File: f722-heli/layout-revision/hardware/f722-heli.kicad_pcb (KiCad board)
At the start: 6 copper layers, 41.7 x 25.4 mm, 156 parts, among them J1 USB4145-03-0170-C, J10 PORT B / JST GH, J11 PORT C / JST GH, J12 DSM / JST ZH, J2 S1 / GND-VX-S, J3 S2 / GND-VX-S, J4 S3 / GND-VX-S, J5 TAIL / GND-VX-S, J6 ESC / GND-VX-S, J7 RPM / GND-VX-S, J8 SBUS / GND-VX-S, J9 PORT A / JST GH, Q1 BSS138LT1G, Q2 BSS138LT1G, SW1 BOOT / KMT031NGJLHS, U1 STM32F722RET6, U10 TPS2553DRVR / USB input limit, U11 TPS2553DRVR / DSM output limit, U12 USBLC6-4SC6 / header clamp, U13 USBLC6-4SC6 / header clamp, U14 TPD4E05U06DQAR / UART ESD, U15 TPD4E05U06DQAR / UART ESD, U16 PESD15VS2UT,215 / 15V ESD, U2 ICM-42688-P, U3 W25N01GVZEIG / 128MiB, U4 DPS368XTSA1 / 0x76, U5 TPS259472ARPWR, U6 TPS63070RNMR / nominal 5.088V, U7 TPS2117DRLR / ABC priority mux, U8 TPS2121RUXR / BEC-priority co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, U9 TPS62162DSGR / 3.3V 1A, Y1 8MHz / CL10pF / TAXM8M4RDBCCT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

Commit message: WIP: checkpoint F722 routing at 49 unfinished connections
Six actual protected channels complete. Current numerical power/VCAP validation pending. Not ready for fabrication or flight.
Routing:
- net SERVO2_MCU: track 0.00 -> 35.8 mm, vias 0 -> 4
- net PORT_C_TX_EXT: track 0.00 -> 19.9 mm, vias 0 -> 2
- net FLASH_HOLD_N: track 0.00 -> 13.4 mm, vias 0 -> 2
- net TAIL_EXT: track 0.00 -> 9.80 mm, vias 0 -> 1
- net PORT_A_TX_EXT: track 0.84 -> 9.07 mm

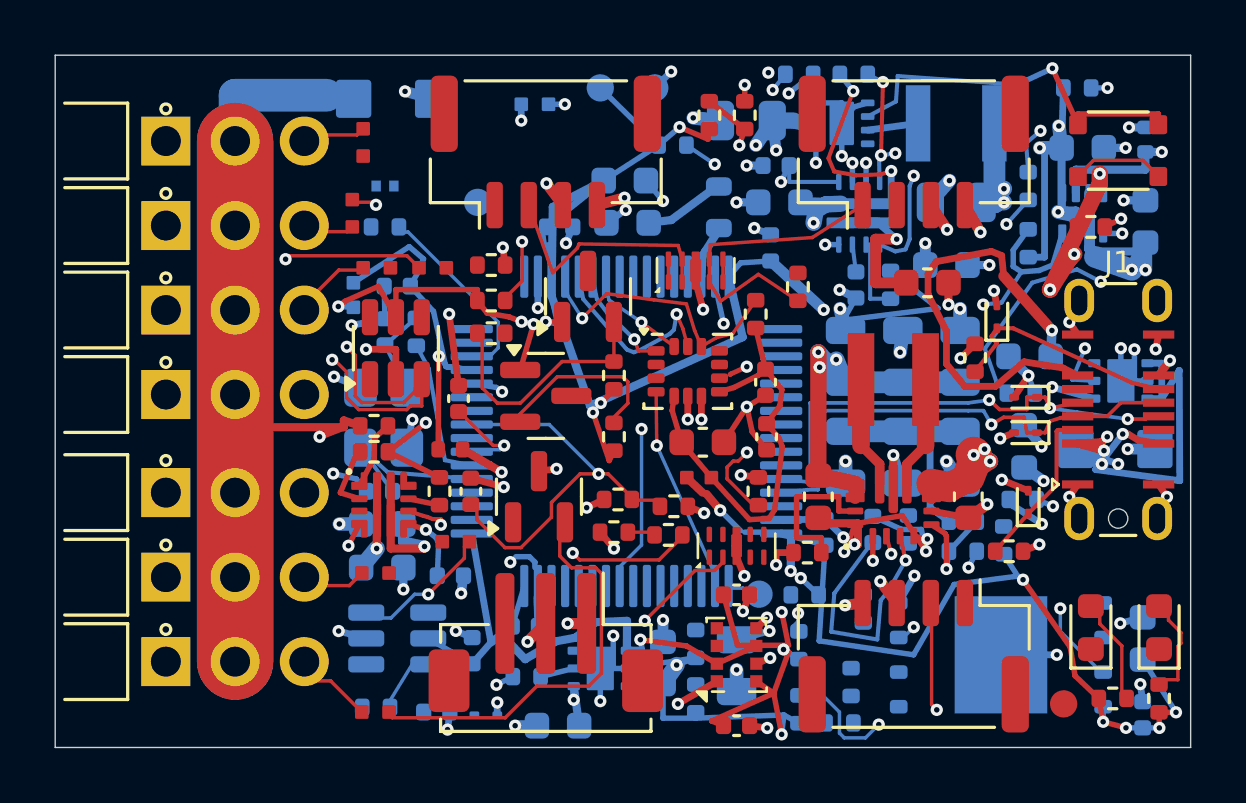
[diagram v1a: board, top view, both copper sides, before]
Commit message: WIP: checkpoint F722 routing at 45 unfinished connections
Native geometry and strict parity clean. Current numerical power/VCAP validation pending. Not ready for fabrication or flight.
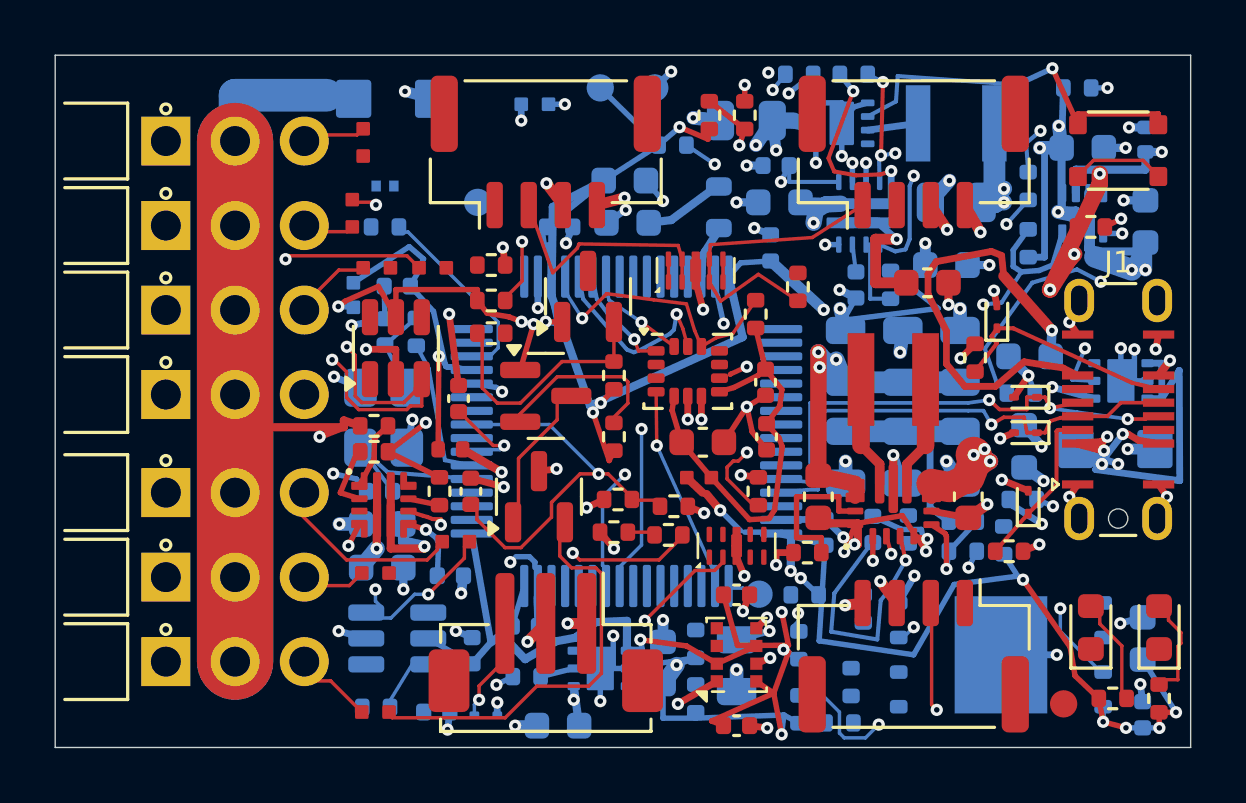
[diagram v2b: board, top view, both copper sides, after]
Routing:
- net ESC_MCU: track 4.39 -> 20.0 mm, vias 1 -> 3
- net ESC_EXT: track 0.00 -> 6.14 mm
- net RPM_HV: track 0.00 -> 4.35 mm
- net DSM_RX_EXT: track 0.00 -> 2.18 mm, vias 0 -> 1
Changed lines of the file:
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@@
+	)
+	(segment
+		(start 16.99961 14.7916)
+		(end 16.99961 16.50142)
+		(width 0.127)
+		(layer "F.Cu")
+		(net "RPM_HV")
+	)
+	(segment
+		(start 16.99961 14.7916)
+		(end 18.41752 13.37369)
+		(width 0.127)
+		(layer "F.Cu")
+		(net "RPM_HV")
+	)
+	(segment
+		(start 18.41752 12.73646)
+		(end 18.41752 13.37369)
+		(width 0.127)
+		(layer "F.Cu")
+		(net "RPM_HV")
 	)
 	(segment
@@
 	)
 	(segment
+		(start 10.68786 18.51864)
+		(end 13.64937 18.51864)
+		(width 0.127)
+		(layer "F.Cu")
+		(net "ESC_EXT")
+	)
+	(segment
+		(start 8.88966 16.72044)
+		(end 10.68786 18.51864)
+		(width 0.127)
+		(layer "F.Cu")
+		(net "ESC_EXT")
+	)
+	(segment
+		(start 13.64937 18.51864)
+		(end 14.01354 18.15447)
+		(width 0.127)
+		(layer "F.Cu")
+		(net "ESC_EXT")
+	)
+	(segment
+		(start 14.01354 18.03646)
+		(end 14.01354 18.15447)
+		(width 0.127)
+		(layer "F.Cu")
+		(net "ESC_EXT")
+	)
+	(segment
 		(start 15.01354 18.03646)
 		(end 15.01354 18.45397)
@@
 	)
 	(via
+		(at 11.75059 19.60158)
+		(size 0.45)
+		(drill 0.2)
+		(layers "F.Cu" "B.Cu")
+		(tenting
+			(front yes)
+			(back yes)
+		)
+		(net "ESC_MCU")
+	)
+	(via
+		(at 20.90574 15.38266)
+		(size 0.45)
+		(drill 0.2)
+		(layers "F.Cu" "B.Cu")
+		(tenting
+			(front yes)
+			(back yes)
+		)
+		(net "ESC_MCU")
+	)
+	(via
 		(at 13.68751 19.78)
 		(size 0.45)
@@
 		(width 0.127)
 		(layer "B.Cu")
+		(net "ESC_MCU")
+	)
+	(segment
+		(start 20.08099 18.71362)
+		(end 20.13148 18.76411)
+		(width 0.127)
+		(layer "B.Cu")
+		(net "ESC_MCU")
+	)
+	(segment
+		(start 20.08099 16.20741)
+		(end 20.08099 18.71362)
+		(width 0.127)
+		(layer "B.Cu")
+		(net "ESC_MCU")
+	)
+	(segment
+		(start 11.75059 19.60158)
+		(end 11.75059 20.02972)
+		(width 0.127)
+		(layer "B.Cu")
+		(net "ESC_MCU")
+	)
+	(segment
+		(start 11.75059 20.02972)
+		(end 11.97126 20.25039)
+		(width 0.127)
+		(layer "B.Cu")
+		(net "ESC_MCU")
+	)
+	(segment
+		(start 20.08099 16.20741)
+		(end 20.90574 15.38266)
+		(width 0.127)
+		(layer "B.Cu")
+		(net "ESC_MCU")
+	)
+	(segment
+		(start 17.40836 19.18389)
+		(end 18.74475 17.8475)
+		(width 0.127)
+		(layer "In2.Cu")
+		(net "ESC_MCU")
+	)
+	(segment
+		(start 12.16828 19.18389)
+		(end 17.40836 19.18389)
+		(width 0.127)
+		(layer "In2.Cu")
+		(net "ESC_MCU")
+	)
+	(segment
+		(start 18.74475 17.8475)
+		(end 18.84039 17.8475)
+		(width 0.127)
+		(layer "In2.Cu")
+		(net "ESC_MCU")
+	)
+	(segment
+		(start 11.75059 19.60158)
+		(end 12.16828 19.18389)
+		(width 0.127)
+		(layer "In2.Cu")
+		(net "ESC_MCU")
+	)
+	(segment
+		(start 20.90574 15.38266)
+		(end 20.90574 15.78215)
+		(width 0.127)
+		(layer "In2.Cu")
+		(net "ESC_MCU")
+	)
+	(segment
+		(start 18.84039 17.8475)
+		(end 20.90574 15.78215)
+		(width 0.127)
+		(layer "In2.Cu")
 		(net "ESC_MCU")
 	)
@@
 	)
 	(segment
+		(start 16.18311 22.50946)
+		(end 16.34054 22.50946)
+		(width 0.127)
+		(layer "F.Cu")
+		(net "DSM_RX_EXT")
+	)
+	(segment
+		(start 15.55286 23.13971)
+		(end 16.18311 22.50946)
+		(width 0.127)
+		(layer "F.Cu")
+		(net "DSM_RX_EXT")
+	)
+	(segment
+		(start 15.55286 23.13971)
+		(end 15.55286 23.65162)
+		(width 0.127)
+		(layer "F.Cu")
+		(net "DSM_RX_EXT")
+	)
+	(via
+		(at 15.55286 23.65162)
+		(size 0.45)
+		(drill 0.2)
+		(layers "F.Cu" "B.Cu")
+		(tenting
+			(front yes)
+			(back yes)
+		)
+		(net "DSM_RX_EXT")
+	)
+	(segment
+		(start 15.38 23.82448)
+		(end 15.38 24.2)
+		(width 0.127)
+		(layer "B.Cu")
+		(net "DSM_RX_EXT")
+	)
+	(segment
+		(start 15.38 23.82448)
+		(end 15.55286 23.65162)
+		(width 0.127)
+		(layer "B.Cu")
+		(net "DSM_RX_EXT")
+	)
+	(segment

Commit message: WIP: checkpoint F722 routing at 14 unfinished connections
Corrected supply-terminal model documented. Current numerical power/VCAP validation pending; historical USB/DSM results invalid. Not for manufacture or flight.
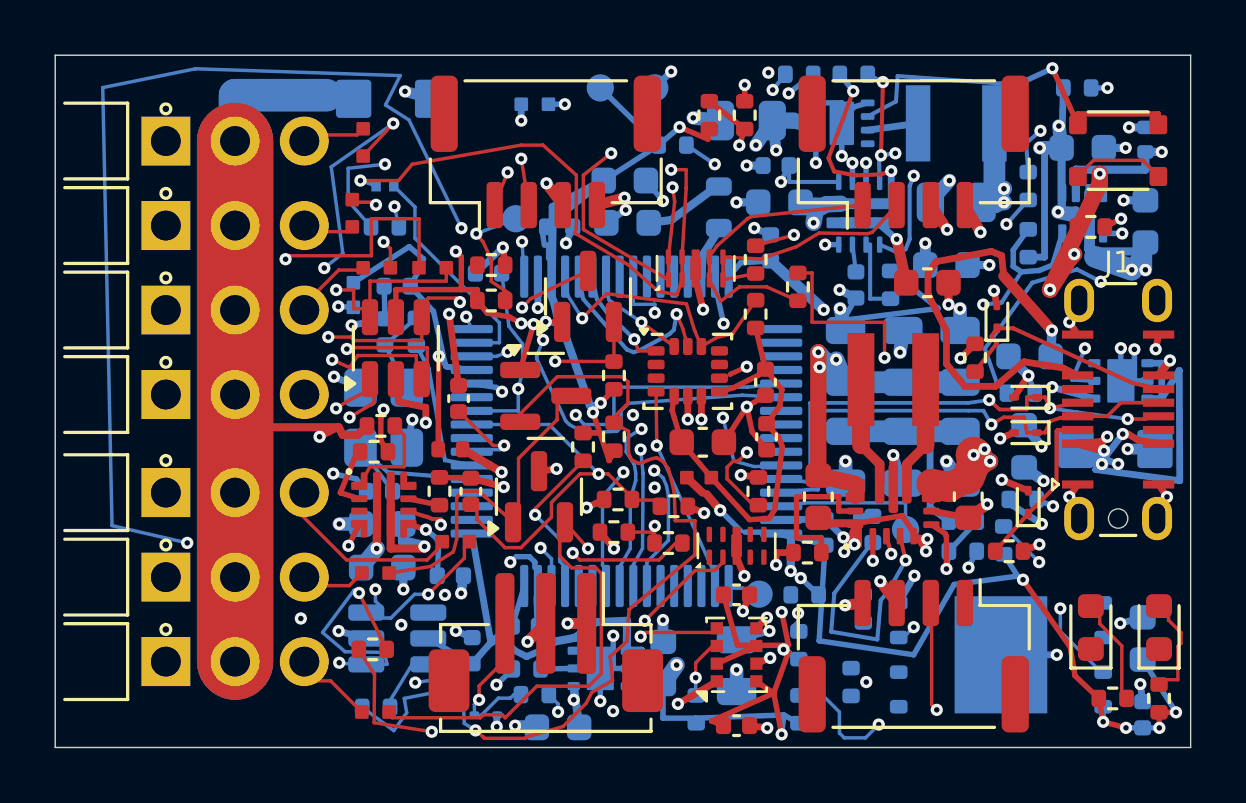
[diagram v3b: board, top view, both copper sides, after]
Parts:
- R33, R7: moved to F.Cu
- TP5: moved to B.Cu
- moved TP5 26.8 mm to (16.9, 6.00)
- moved TP1 19.8 mm to (31.2, 17.4)
- moved C31 16.2 mm to (15.9, 8.00), turned to 180 degrees
- moved R45 12.4 mm to (11.7, 21.8)
- moved R33 11.4 mm to (25.7, 7.50)
- moved R38 11.2 mm to (17.6, 23.5)
- moved R7 8.32 mm to (19.4, 14.4), turned to -90 degrees
- moved R8 0.40 mm to (23.5, 24.0)
- moved R43 0.30 mm to (22.5, 17.9)
- moved R70 0.28 mm to (17.3, 22.5)
- moved R50 0.25 mm to (11.9, 13.6)
- moved U14 0.08 mm to (23.5, 7.83)
- moved C70 0.06 mm to (18.4, 24.7)
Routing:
- net TAIL_MCU: track 0.00 -> 85.7 mm, vias 0 -> 4
- net SBUS_LV: track 7.82 -> 75.6 mm, vias 0 -> 2
- net RPM_MCU: track 1.56 -> 59.4 mm, vias 0 -> 5
- net DSM_RX_MCU: track 0.00 -> 55.0 mm, vias 0 -> 5
- net SBUS_MCU: track 0.00 -> 51.0 mm, vias 0 -> 3
- net SERVO1_MCU: track 0.00 -> 44.1 mm, vias 0 -> 5
- net PORT_A_RX_EXT: track 0.84 -> 35.2 mm, vias 0 -> 4
- net PORT_B_TX_MCU: track 0.00 -> 33.0 mm, vias 0 -> 2
- net PORT_B_RX_MCU: track 0.00 -> 27.3 mm, vias 0 -> 2
- net RPM_LV: track 6.41 -> 32.3 mm, vias 0 -> 1
- net BARO_SDA: track 0.00 -> 22.6 mm, vias 0 -> 3
- net SERVO3_MCU: track 0.00 -> 21.7 mm, vias 0 -> 4
- net PORT_A_TX_EXT: track 9.07 -> 29.3 mm, vias 0 -> 3
- net BARO_SCL: track 0.00 -> 19.6 mm, vias 0 -> 3
- net SBUS_HV: track 14.6 -> 33.3 mm, vias 0 -> 2
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
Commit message: WIP: checkpoint F722 at 13 unfinished connections
Native geometry/parity/ERC clean; exact reference-hole boundary conflicts retained. Current numerical power/VCAP and hardware qualification pending.
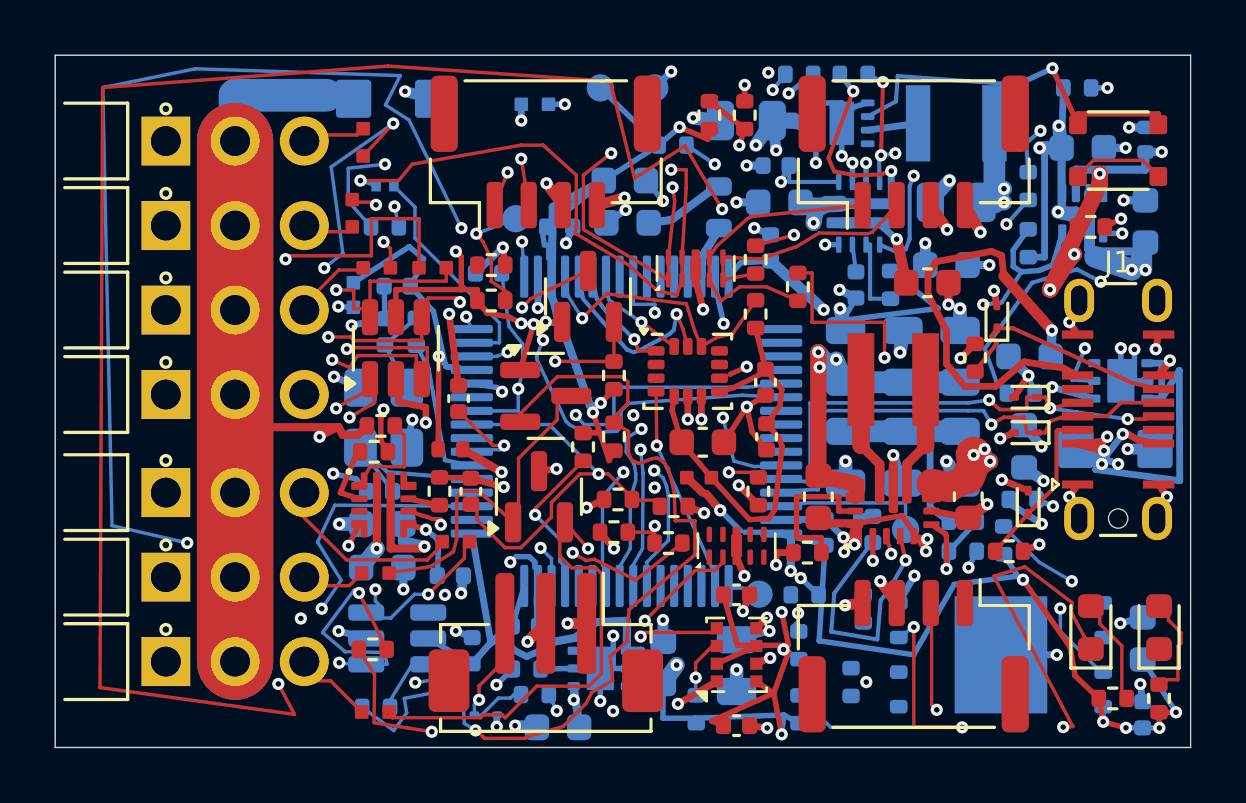
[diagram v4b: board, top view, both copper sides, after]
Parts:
- turned R44 to -90 degrees
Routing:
- net DSM_RX_MCU: track 55.0 -> 139.9 mm
- net LED_GREEN_K: track 0.00 -> 71.9 mm, vias 0 -> 3
- net FLASH_HOLD_N: track 13.4 -> 21.3 mm
- net FLASH_WP_N: track 9.04 -> 12.6 mm
- net ADC_DIV_MID: track 15.5 -> 13.6 mm
- net ADC_BUS: track 18.1 -> 17.4 mm

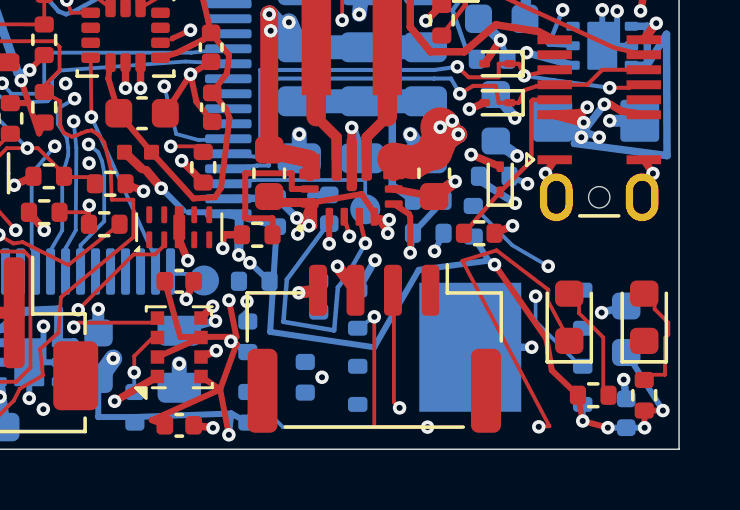
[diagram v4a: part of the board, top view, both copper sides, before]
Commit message: WIP: checkpoint F722 at 12 unfinished connections
Native geometry/parity/ERC clean. Current numerical power/VCAP and complete CS timing pending. Not for manufacture or flight.
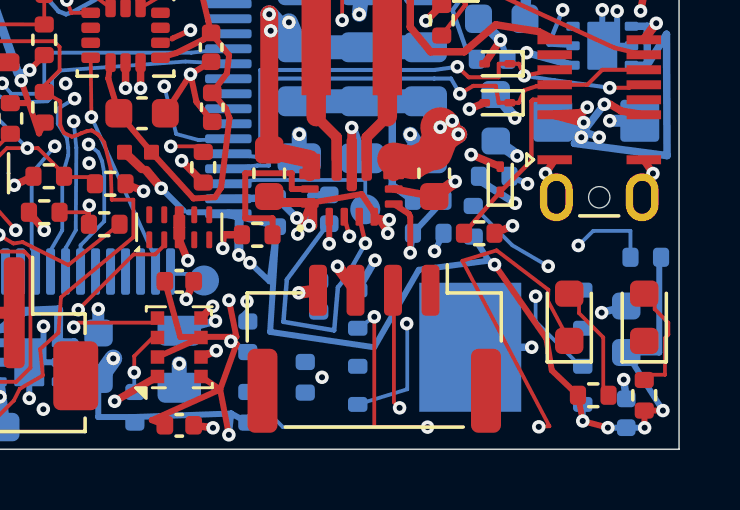
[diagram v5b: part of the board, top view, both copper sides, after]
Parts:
- moved R4 13.1 mm to (40.5, 19.0)
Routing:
- net FLASH_CS: track 0.00 -> 14.0 mm, vias 0 -> 2
- net +3V3_CORE: track 213.9 -> 220.1 mm
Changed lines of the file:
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@@
 	(footprint "F722_Heli:R_0402_1005Metric"
 		(layer "B.Cu")
-		(at 27.5 19.8 180)
+		(at 40.55 19 180)
 		(descr "Resistor SMD 0402 (1005 Metric), square (rectangular) end terminal, IPC-7351 nominal, (Body size source: IPC-SM-782 page 72, https://www.pcb-3d.com/wordpress/wp-content/uploads/ipc-sm-782a_amendment_1_and_2.pdf), generated with kicad-footprint-generator")
 		(tags "resistor")
@@
 	)
 	(segment
+		(start 41.06 19)
+		(end 41 19)
+		(width 0.2)
+		(layer "B.Cu")
+		(net "+3V3_CORE")
+	)
+	(segment
 		(start 27.355841 19.183513)
 		(end 28.01 19.8)
@@
 	)
 	(segment
+		(start 41 19)
+		(end 41 22.175)
+		(width 0.2)
+		(layer "B.Cu")
+		(net "+3V3_CORE")
+	)
+	(segment
 		(start 18.257041 5.566991)
 		(end 20.125 4.6)
@@
 	)
 	(segment
+		(start 28.01 19.8)
+		(end 28.25 17.98)
+		(width 0.2)
+		(layer "B.Cu")
+		(net "+3V3_CORE")
+	)
+	(segment
 		(start 39.9 24.68)
 		(end 40.51235 24.682349)
@@
 	)
 	(segment
+		(start 41 22.175)
+		(end 39.9 22.175)
+		(width 0.2)
+		(layer "B.Cu")
+		(net "+3V3_CORE")
+	)
+	(segment
 		(start 19.622698 12.867203)
 		(end 20.017207 12.759784)
@@
 		(net "DSM_RX_MCU")
 	)
+	(via
+		(at 38.300522 18.607676)
+		(size 0.45)
+		(drill 0.2)
+		(layers "F.Cu" "B.Cu")
+		(tenting
+			(front yes)
+			(back yes)
+		)
+		(net "FLASH_CS")
+	)
+	(via
+		(at 32.582039 21.210477)
+		(size 0.45)
+		(drill 0.2)
+		(layers "F.Cu" "B.Cu")
+		(tenting
+			(front yes)
+			(back yes)
+		)
+		(net "FLASH_CS")
+	)
+	(segment
+		(start 38.300522 18.607676)
+		(end 38.8 18.12)
+		(width 0.127)
+		(layer "B.Cu")
+		(net "FLASH_CS")
+	)
+	(segment
+		(start 40.04 18.12)
+		(end 40.04 19)
+		(width 0.127)
+		(layer "B.Cu")
+		(net "FLASH_CS")
+	)
+	(segment
+		(start 32.6 21.4)
+		(end 32.582039 21.210477)
+		(width 0.127)
+		(layer "B.Cu")
+		(net "FLASH_CS")
+	)
+	(segment
+		(start 38.8 18.12)
+		(end 40.04 18.12)
+		(width 0.127)
+		(layer "B.Cu")
+		(net "FLASH_CS")
+	)
+	(segment
+		(start 32.6 23.4)
+		(end 32.6 21.4)
+		(width 0.127)
+		(layer "B.Cu")
+		(net "FLASH_CS")
+	)
+	(segment
+		(start 30.95 23.905)
+		(end 32.6 23.4)
+		(width 0.127)
+		(layer "B.Cu")
+		(net "FLASH_CS")
+	)
+	(segment
+		(start 37.148066 19.777476)
+		(end 38.394367 19.836498)
+		(width 0.127)
+		(layer "In2.Cu")
+		(net "FLASH_CS")
+	)
+	(segment
+		(start 38.394367 19.836498)
+		(end 38.300522 18.607676)
+		(width 0.127)
+		(layer "In2.Cu")
+		(net "FLASH_CS")
+	)
+	(segment
+		(start 32.582039 21.210477)
+		(end 37.148066 19.777476)
+		(width 0.127)
+		(layer "In2.Cu")
+		(net "FLASH_CS")
+	)
 	(segment
